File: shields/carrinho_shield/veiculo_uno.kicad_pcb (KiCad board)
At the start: 2 copper layers, 68.6 x 53.3 mm, 29 parts, among them J1 Conn_01x26_Male, J10 Conn_01x02_Male, J11 Conn_01x02_Male, J12 Conn_01x02_Male, J13 Conn_01x02_Male, J14 Conn_01x02_Male, J15 Conn_01x02_Male, J16 Conn_01x02_Male, J17 Conn_01x02_Male, J18 Conn_01x02_Male, J19 Conn_01x02_Male, J2 Conn_01x02_Male, J20 Conn_01x02_Male, J21 Conn_01x02_Male, J3 Conn_01x02_Male, J4 Conn_01x02_Male, J5 Conn_01x02_Male, J6 Conn_01x02_Male, J7 Conn_01x02_Male, J8 Conn_01x02_Male, J9 Conn_01x02_Male, P1 Power, P2 Analog, P3 Digital, P4 Digital, P5 CONN_01X01, P6 CONN_01X01, P7 CONN_01X01, P8 CONN_01X01

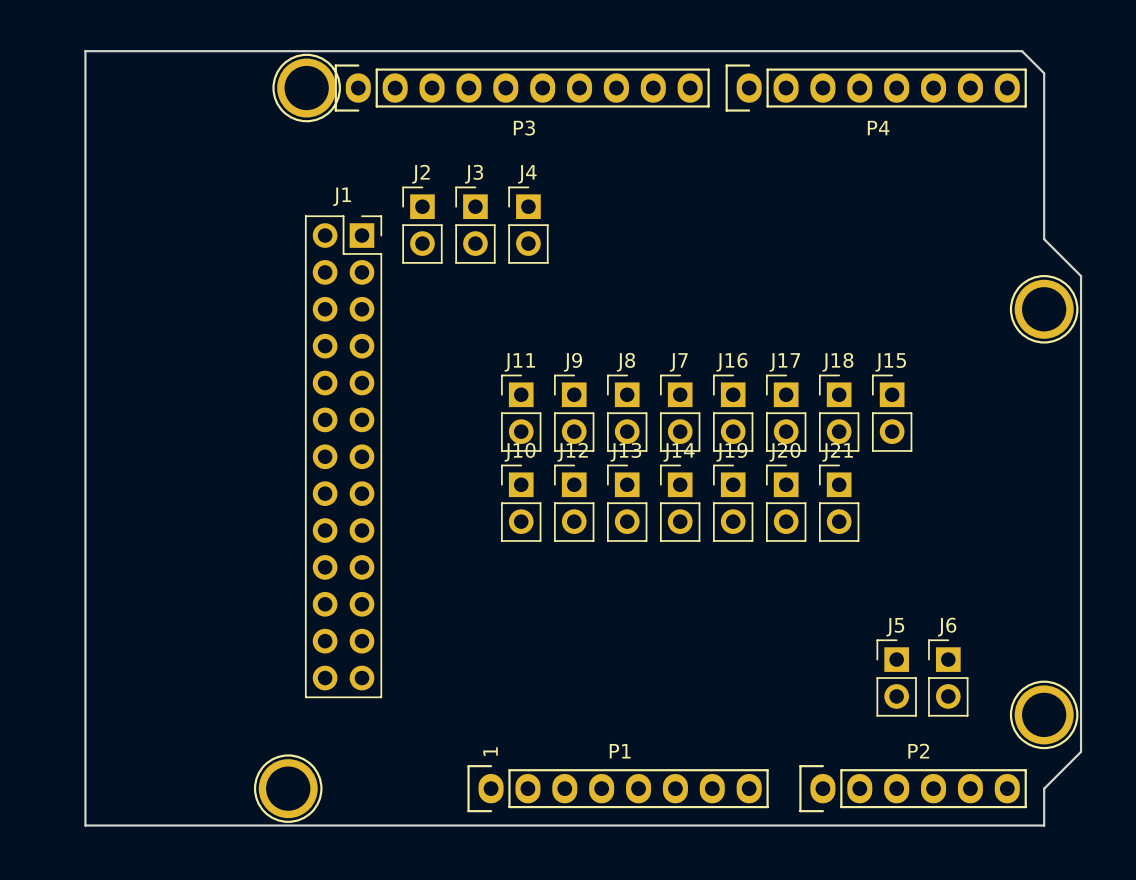
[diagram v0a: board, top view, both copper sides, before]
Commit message: Added shield schematic
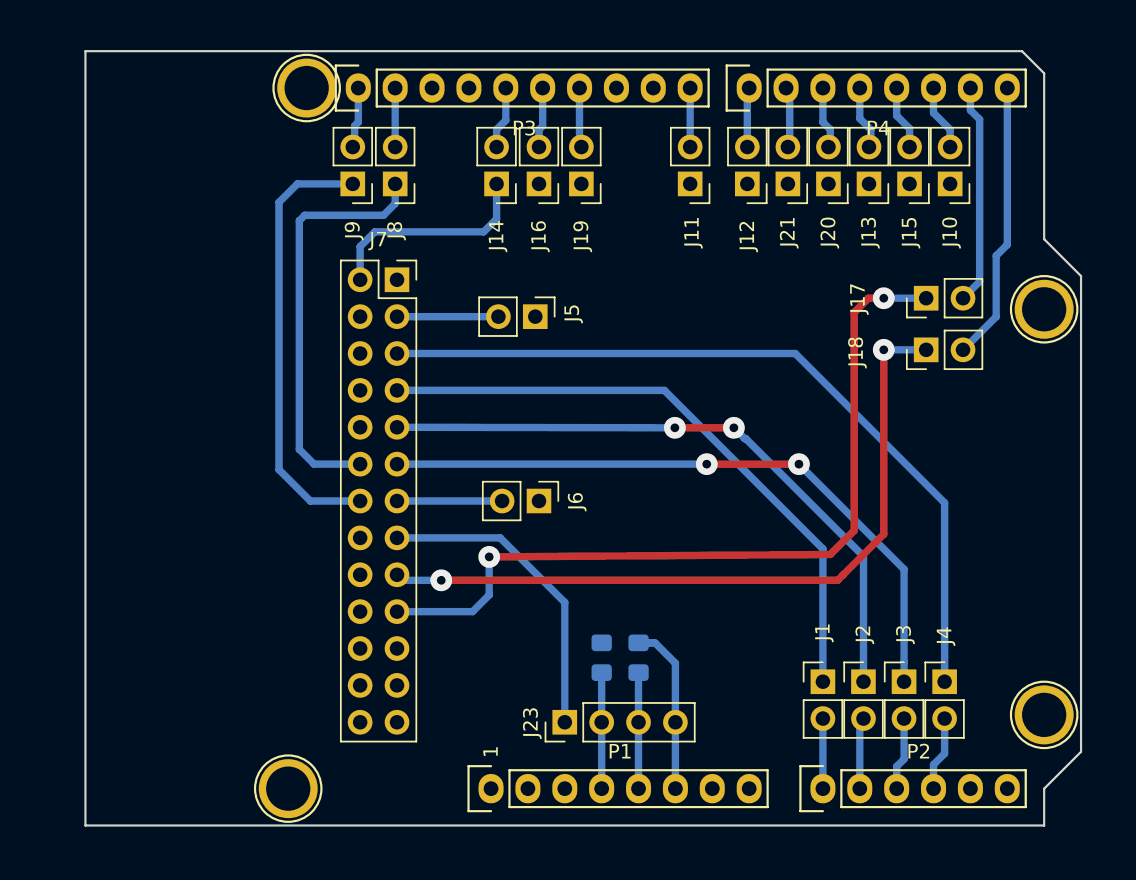
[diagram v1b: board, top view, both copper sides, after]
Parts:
- added C1: 100n, Capacitor_SMD:C_0805_2012Metric_Pad1.15x1.40mm_HandSolder, B.Cu at (149.1, 114.8)
- added C2: 100n, Capacitor_SMD:C_0805_2012Metric_Pad1.15x1.40mm_HandSolder, B.Cu at (146.6, 114.8)
- added J23: Conn_01x04_Male, Connector_PinHeader_2.54mm:PinHeader_1x04_P2.54mm_Vertical, F.Cu at (144.0, 119.3)
- J1: value Conn_01x26_Male -> Conn_01x02_Male; footprint Connector_PinSocket_2.54mm:PinSocket_2x13_P2.54mm_Vertical -> Connector_PinHeader_2.54mm:PinHeader_1x02_P2.54mm_Vertical
- J7: value Conn_01x02_Male -> Conn_02x13_Odd_Even; footprint Connector_PinHeader_2.54mm:PinHeader_1x02_P2.54mm_Vertical -> Connector_PinSocket_2.54mm:PinSocket_2x13_P2.54mm_Vertical
- moved J2 44.6 mm to (164.6, 116.5)
- moved J1 44.2 mm to (161.8, 116.5)
- moved J3 44.1 mm to (167.4, 116.5)
- moved J4 43.5 mm to (170.2, 116.5)
- moved J10 36.1 mm to (170.6, 82.2), turned to 180 degrees
- moved J5 34.3 mm to (142.0, 91.3), turned to 270 degrees
- moved J6 30.2 mm to (142.2, 104.0), turned to 270 degrees
- moved J13 26.6 mm to (165.0, 82.2), turned to 180 degrees
- moved J14 24.3 mm to (139.3, 82.2), turned to 180 degrees
- moved J12 23.9 mm to (156.6, 82.2), turned to 180 degrees
- moved J19 23.2 mm to (145.2, 82.2), turned to 180 degrees
- moved J8 21.6 mm to (132.3, 82.2), turned to 180 degrees
- moved J9 21.1 mm to (129.4, 82.2), turned to 180 degrees
- moved J7 21.1 mm to (132.5, 88.8)
- moved J21 21.0 mm to (159.4, 82.2), turned to 180 degrees
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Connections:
- J1 pad 1: GND -> ADC0
- J1 pad 2: Net-(J1-Pad2) -> A0
- J10 pad 1: Trig0 -> Echo1
- J10 pad 2: 9 -> 2
- J11 pad 1: ADC0 -> Echo0
- J11 pad 2: A0 -> 8
- J12 pad 1: RXB -> Trig0
- J12 pad 2: Tx -> 7
- J13 pad 1: PWM2 -> Trig1
- J13 pad 2: 11 -> 4
- J14 pad 1: Trig1 -> D0
- J14 pad 2: 2 -> 13
- J16 pad 1: TXB -> D1
- J16 pad 2: Rx -> 12
- J17 pad 1: PWM1N -> RXB
- J17 pad 2: 5 -> Tx
- J18 pad 1: D0 -> TXB
- J18 pad 2: 13 -> Rx
- J19 pad 1: D1 -> PWM2
- J19 pad 2: 12 -> 11
- J2 pad 1: Echo1 -> ADC1
- J2 pad 2: 4 -> A1
- J20 pad 1: ADC2 -> PWM1N
- J20 pad 2: A2 -> 5
- J3 pad 1: R_TCRT -> ADC2
- J3 pad 2: 10 -> A2
- J4 pad 1: Echo0 -> ADC3
- J4 pad 2: 8 -> A3
- J5 pad 1: ADC1 -> GND
- J5 pad 2: A1 -> AMP1
- J6 pad 1: ADC3 -> GND
- J6 pad 2: A3 -> AMP2
- J7 pad 1: A2' -> GND
- J7 pad 2: Conector -> D0
- J8 pad 1: A1' -> R_TCRT
- J8 pad 2: Conector' -> A4(SDA)
- J9 pad 2: 7 -> A5(SCL)
- P2 pad 5: /A4(SDA) -> A4(SDA)
- P2 pad 6: /A5(SCL) -> A5(SCL)
- P3 pad 1: /A5(SCL) -> A5(SCL)
- P3 pad 2: /A4(SDA) -> A4(SDA)
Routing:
- net RXB: track 0.00 -> 55.8 mm, vias 0 -> 2
- net ADC3: track 0.00 -> 54.3 mm
- net TXB: track 0.00 -> 50.6 mm, vias 0 -> 2
- net ADC2: track 0.00 -> 45.7 mm, vias 0 -> 2
- net ADC1: track 0.00 -> 44.5 mm, vias 0 -> 2
- net ADC0: track 0.00 -> 43.0 mm
- net L_TCRT: track 0.00 -> 30.5 mm
- net +5V: track 0.00 -> 29.6 mm
- net R_TCRT: track 0.00 -> 28.8 mm
- net Rx: track 0.00 -> 19.3 mm
- net Tx: track 0.00 -> 15.2 mm
- net D0: track 0.00 -> 14.9 mm
- net GND: track 0.00 -> 11.8 mm
- net +3V3: track 0.00 -> 7.99 mm
- net AMP2: track 0.00 -> 7.24 mm
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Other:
- net class Default: clearance 0.2 -> 0.3048; trace_width 0.25 -> 0.508; via_dia 0.6 -> 1.5; via_drill 0.4 -> 0.6
- rule trace_clearance: 0.2 -> 0.3048

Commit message: Done PCI layout
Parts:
- removed J18: Conn_01x02_Male, Connector_PinHeader_2.54mm:PinHeader_1x02_P2.54mm_Vertical
- removed P5: CONN_01X01, Socket_Arduino_Uno:Arduino_1pin
- added D1: LED, LED_SMD:LED_0805_2012Metric, F.Cu at (150.3, 111.9)
- added R1: R, Resistor_SMD:R_0805_2012Metric, F.Cu at (154.7, 112.8)
- added RX: Conn_01x02_Male, Connector_PinHeader_2.54mm:PinHeader_1x02_P2.54mm_Vertical, F.Cu at (168.9, 93.6)
- ECHO 1: renamed from J10
- L DIR: renamed from J8
- L ESQ: renamed from J9
- moved ADC0 5.59 mm to (167.4, 116.5)
- moved ADC2 5.59 mm to (161.8, 116.5)
- moved AMP2 4.58 mm to (140.7, 108.3)
- moved AMP1 4.47 mm to (140.8, 95.6)
- moved J7 4.32 mm to (132.3, 93.1)
- moved C1 1.63 mm to (150.4, 115.8), turned to 0 degrees
- renumbered J4 to ACD3, J1 to ADC0, J2 to ADC1, J3 to ADC2, J5 to AMP1, J6 to AMP2, J11 to ECHO0, J14 to ENC0, J16 to ENC1, J21 to M1, J20 to M1N, J19 to M2, J15 to M2N, J12 to TRIG0, J13 to TRIG1, J17 to TX
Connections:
- ADC0 pad 2: A0 -> A2
- ADC2 pad 2: A2 -> A0
- J7 pad 18: Net-(J7-Pad18) -> GND
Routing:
- net PWM1: track 0.00 -> 107.5 mm, vias 0 -> 1
- net PWM2N: track 0.00 -> 97.1 mm, vias 0 -> 1
- net PWM2: track 0.00 -> 87.7 mm, vias 0 -> 2
- net Echo0: track 0.00 -> 81.8 mm
- net Trig0: track 0.00 -> 81.5 mm
- net D1: track 0.00 -> 79.9 mm
- net Echo1: track 0.00 -> 73.4 mm
- net PWM1N: track 0.00 -> 61.1 mm, vias 0 -> 3
- net Trig1: track 0.00 -> 60.0 mm, vias 0 -> 3
- net +5V: track 29.6 -> 40.8 mm, vias 0 -> 3
- net ADC2: track 45.7 -> 37.5 mm, vias 2 -> 0
- net ADC3: track 54.3 -> 46.2 mm
- net GND: track 11.8 -> 16.1 mm, vias 0 -> 1
- net ADC1: track 44.5 -> 40.4 mm, vias 2 -> 0
- net D0: track 14.9 -> 18.5 mm
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- added copper zone on B.Cu, net GND
- added copper zone on F.Cu, net GND

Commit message: Added level converter RX / TX signals
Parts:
- removed ACD3, ADC0, ADC1, ADC2, AMP1, AMP2, ECHO0, ENC0, ENC1, M1, M1N, M2, M2N, RX, TRIG0, TRIG1, TX: Conn_01x02_Male, Connector_PinHeader_2.54mm:PinHeader_1x02_P2.54mm_Vertical
- removed ECHO 1: Conn_01x02_Male, Connector_PinHeader_2.54mm:PinHeader_1x02_P2.54mm_Vertical
- removed L DIR: Conn_01x02_Male, Connector_PinHeader_2.54mm:PinHeader_1x02_P2.54mm_Vertical
- removed L ESQ: Conn_01x02_Male, Connector_PinHeader_2.54mm:PinHeader_1x02_P2.54mm_Vertical
- added J1: Conn_01x02_Male, Connector_PinHeader_2.54mm:PinHeader_1x02_P2.54mm_Vertical, F.Cu at (167.4, 116.4)
- added J10: Conn_01x02_Male, Connector_PinHeader_2.54mm:PinHeader_1x02_P2.54mm_Vertical, F.Cu at (170.9, 81.7)
- added J11: Conn_01x02_Male, Connector_PinHeader_2.54mm:PinHeader_1x02_P2.54mm_Vertical, F.Cu at (152.6, 81.7)
- added J12: Conn_01x02_Male, Connector_PinHeader_2.54mm:PinHeader_1x02_P2.54mm_Vertical, F.Cu at (156.6, 81.7)
- added J13: Conn_01x02_Male, Connector_PinHeader_2.54mm:PinHeader_1x02_P2.54mm_Vertical, F.Cu at (165.1, 81.7)
- added J14: Conn_01x02_Male, Connector_PinHeader_2.54mm:PinHeader_1x02_P2.54mm_Vertical, F.Cu at (139.3, 81.7)
- added J15: Conn_01x02_Male, Connector_PinHeader_2.54mm:PinHeader_1x02_P2.54mm_Vertical, F.Cu at (167.9, 81.7)
- added J16: Conn_01x02_Male, Connector_PinHeader_2.54mm:PinHeader_1x02_P2.54mm_Vertical, F.Cu at (142.2, 81.7)
- added J17: Conn_01x02_Male, Connector_PinHeader_2.54mm:PinHeader_1x02_P2.54mm_Vertical, F.Cu at (162.9, 95.8)
- added J18: Conn_01x02_Male, Connector_PinHeader_2.54mm:PinHeader_1x02_P2.54mm_Vertical, F.Cu at (162.9, 100.1)
- added J19: Conn_01x02_Male, Connector_PinHeader_2.54mm:PinHeader_1x02_P2.54mm_Vertical, F.Cu at (145.1, 81.7)
- added J2: Conn_01x02_Male, Connector_PinHeader_2.54mm:PinHeader_1x02_P2.54mm_Vertical, F.Cu at (164.5, 116.4)
- added J20: Conn_01x02_Male, Connector_PinHeader_2.54mm:PinHeader_1x02_P2.54mm_Vertical, F.Cu at (162.3, 81.7)
- added J21: Conn_01x02_Male, Connector_PinHeader_2.54mm:PinHeader_1x02_P2.54mm_Vertical, F.Cu at (159.5, 81.7)
- added J3: Conn_01x02_Male, Connector_PinHeader_2.54mm:PinHeader_1x02_P2.54mm_Vertical, F.Cu at (161.7, 116.3)
- added J4: Conn_01x02_Male, Connector_PinHeader_2.54mm:PinHeader_1x02_P2.54mm_Vertical, F.Cu at (170.2, 116.4)
- added J5: Conn_01x02_Male, Connector_PinHeader_2.54mm:PinHeader_1x02_P2.54mm_Vertical, F.Cu at (140.9, 95.6)
- added J6: Conn_01x02_Male, Connector_PinHeader_2.54mm:PinHeader_1x02_P2.54mm_Vertical, F.Cu at (140.9, 108.3)
- added J8: Conn_01x02_Male, Connector_PinHeader_2.54mm:PinHeader_1x02_P2.54mm_Vertical, F.Cu at (132.5, 81.7)
- added J9: Conn_01x02_Male, Connector_PinHeader_2.54mm:PinHeader_1x02_P2.54mm_Vertical, F.Cu at (129.4, 81.7)
- added Q1: 2N7002, Package_TO_SOT_SMD:SOT-23, B.Cu at (169.0, 91.0)
- added Q2: 2N7002, Package_TO_SOT_SMD:SOT-23, B.Cu at (169.3, 102.0)
- added R2: 2k2, Resistor_SMD:R_0805_2012Metric, B.Cu at (169.0, 94.1)
- added R3: 2k2, Resistor_SMD:R_0805_2012Metric, B.Cu at (170.0, 87.8)
- added R4: 2k2, Resistor_SMD:R_0805_2012Metric, B.Cu at (169.3, 105.5)
- added R5: 2k2, Resistor_SMD:R_0805_2012Metric, B.Cu at (170.3, 99.0)
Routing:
- net +3V3: track 7.99 -> 59.4 mm, vias 0 -> 3
- net +5V: track 40.8 -> 86.9 mm, vias 3 -> 7
- net RXB: track 55.4 -> 45.5 mm
- net Rx: track 19.3 -> 27.8 mm
- net Net-(J18-Pad2): track 0.00 -> 7.31 mm
- net TXB: track 50.9 -> 43.9 mm
- net Net-(J17-Pad2): track 0.00 -> 5.41 mm
- net Tx: track 15.2 -> 17.2 mm

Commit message: Added aligment holes
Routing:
- net GND: vias 1 -> 3
- net (no net): vias 0 -> 1
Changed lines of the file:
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@@
-(kicad_pcb (version 20171130) (host pcbnew 5.0.2+dfsg1-1)
+(kicad_pcb (version 20171130) (host pcbnew 5.1.5-5.1.5)
   (general
     (thickness 1.6)
-    (drawings 27)
-    (tracks 303)
+    (drawings 32)
+    (tracks 306)
     (zones 0)
     (modules 39)
@@
     (zone_45_only no)
     (trace_min 0.2)
-    (segment_width 0.15)
-    (edge_width 0.15)
     (via_size 1.5)
     (via_drill 0.6)
@@
     (uvia_min_size 0.2)
     (uvia_min_drill 0.1)
+    (edge_width 0.15)
+    (segment_width 0.15)
     (pcb_text_width 0.3)
     (pcb_text_size 1.5 1.5)
@@
     )
   )
+  (target plus (at 112.268 99.695) (size 2) (width 0.15) (layer Edge.Cuts))
+  (target plus (at 175.768 99.695) (size 2) (width 0.15) (layer Edge.Cuts))
+  (gr_line (start 177.038 99.695) (end 107.188 99.695) (layer F.SilkS) (width 0.15))
+  (dimension 26.67 (width 0.15) (layer F.SilkS)
+    (gr_text "26.670 mm" (at 202.468 86.36 270) (layer F.SilkS)
+      (effects (font (size 1 1) (thickness 0.15)))
+    )
+    (feature1 (pts (xy 174.498 99.695) (xy 201.754421 99.695)))
+    (feature2 (pts (xy 174.498 73.025) (xy 201.754421 73.025)))
+    (crossbar (pts (xy 201.168 73.025) (xy 201.168 99.695)))
+    (arrow1a (pts (xy 201.168 99.695) (xy 200.581579 98.568496)))
+    (arrow1b (pts (xy 201.168 99.695) (xy 201.754421 98.568496)))
+    (arrow2a (pts (xy 201.168 73.025) (xy 200.581579 74.151504)))
+    (arrow2b (pts (xy 201.168 73.025) (xy 201.754421 74.151504)))
+  )
+  (dimension 53.34 (width 0.15) (layer F.SilkS)
+    (gr_text "53.340 mm" (at 193.578 99.695 270) (layer F.SilkS)
+      (effects (font (size 1 1) (thickness 0.15)))
+    )
+    (feature1 (pts (xy 174.498 126.365) (xy 192.864421 126.365)))
+    (feature2 (pts (xy 174.498 73.025) (xy 192.864421 73.025)))
+    (crossbar (pts (xy 192.278 73.025) (xy 192.278 126.365)))
+    (arrow1a (pts (xy 192.278 126.365) (xy 191.691579 125.238496)))
+    (arrow1b (pts (xy 192.278 126.365) (xy 192.864421 125.238496)))
+    (arrow2a (pts (xy 192.278 73.025) (xy 191.691579 74.151504)))
+    (arrow2b (pts (xy 192.278 73.025) (xy 192.864421 74.151504)))
+  )
   (gr_line (start 179.578 88.519) (end 177.038 85.979) (angle 90) (layer Edge.Cuts) (width 0.15))
   (gr_line (start 178.435 94.615) (end 178.435 102.235) (angle 90) (layer Dwgs.User) (width 0.15))
@@
   (gr_line (start 120.523 82.55) (end 120.523 93.98) (angle 90) (layer Dwgs.User) (width 0.15))
   (gr_line (start 104.648 82.55) (end 120.523 82.55) (angle 90) (layer Dwgs.User) (width 0.15))
+  (via (at 110.998 126.365) (size 1.5) (drill 0.6) (layers F.Cu B.Cu) (net 0))
   (segment (start 149.098 119.253) (end 149.098 123.825) (width 0.508) (layer B.Cu) (net 3))
   (segment (start 149.098 119.253) (end 149.098 115.833) (width 0.508) (layer B.Cu) (net 3))
@@
   (segment (start 129.794 95.631) (end 122.301 95.631) (width 0.508) (layer F.Cu) (net 4))
   (via (at 122.301 95.631) (size 1.5) (drill 0.6) (layers F.Cu B.Cu) (net 4))
+  (via (at 112.268 99.695) (size 1.5) (drill 0.6) (layers F.Cu B.Cu) (net 4))
+  (via (at 175.768 99.695) (size 1.5) (drill 0.6) (layers F.Cu B.Cu) (net 4))
   (segment (start 146.558 123.825) (end 146.558 119.253) (width 0.508) (layer B.Cu) (net 11))
   (segment (start 169.988 94.08) (end 169.983 94.085) (width 0.508) (layer B.Cu) (net 11))
